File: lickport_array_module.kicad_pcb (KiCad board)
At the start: 2 copper layers, 74.9 x 80.6 mm, 105 parts, among them P1 PWR_JACK_2.1x5.5_SMD_RA, SW1 SPDT_SLIDE_500A_SM, U1 DRV103, U2 DRV103, U3 DRV103, U4 DRV103, U5 DRV103, U6 DRV103, U7 DRV103, U8 DRV103, U9 DRV103

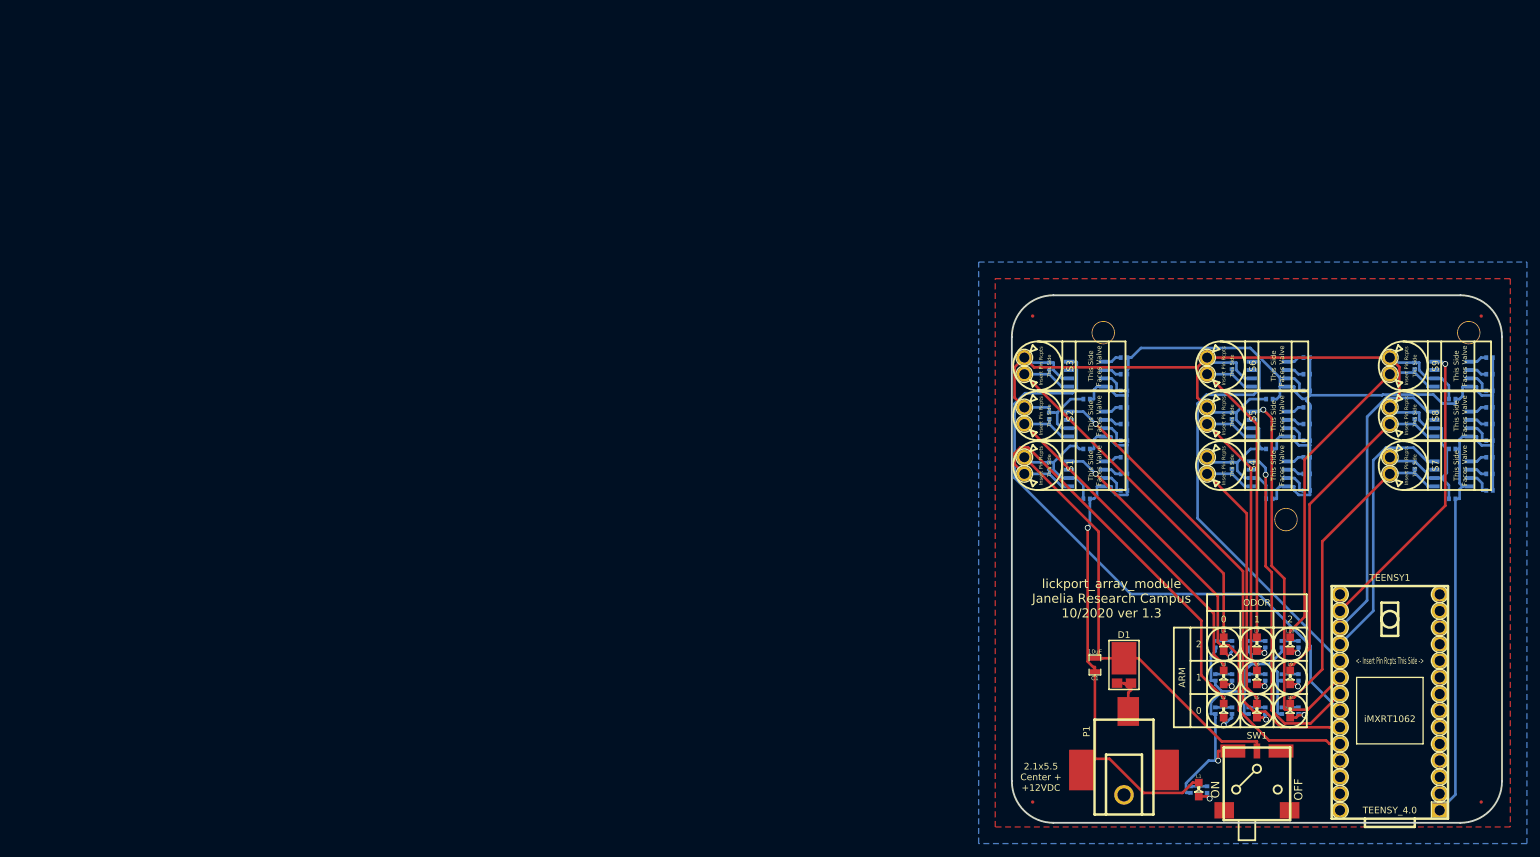
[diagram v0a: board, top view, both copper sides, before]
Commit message: Update version numbers
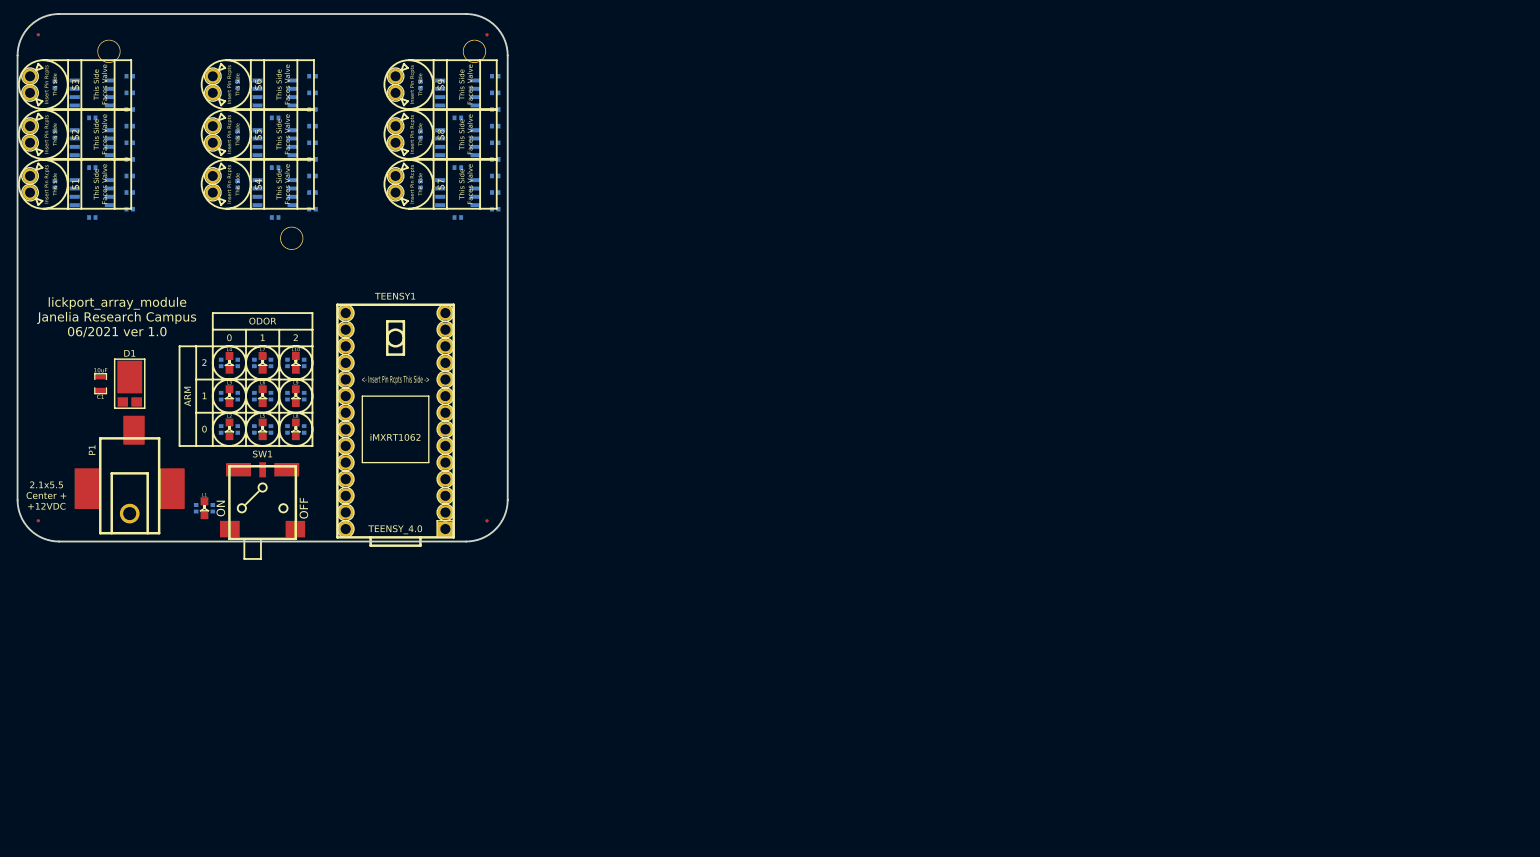
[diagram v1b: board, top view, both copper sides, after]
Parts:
- moved C1 158.0 mm to (-88.5, 64.3)
- moved C10 158.0 mm to (-61.8, 31.3)
- moved C11 158.0 mm to (-56.1, 27.5)
- moved C12 158.0 mm to (-61.8, 23.7)
- moved C13 158.0 mm to (-56.1, 19.9)
- moved C14 158.0 mm to (-33.9, 38.9)
- moved C15 158.0 mm to (-28.2, 35.1)
- moved C16 158.0 mm to (-33.9, 31.3)
- moved C17 158.0 mm to (-28.2, 27.5)
- moved C18 158.0 mm to (-33.9, 23.7)
- moved C19 158.0 mm to (-28.2, 19.9)
- moved C2 158.0 mm to (-89.8, 38.9)
- moved C3 158.0 mm to (-84.1, 35.1)
- moved C4 158.0 mm to (-89.8, 31.3)
- moved C5 158.0 mm to (-84.1, 27.5)
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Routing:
- net GND: track 300.6 -> 0.00 mm, vias 1 -> 0
- net VCC: track 286.7 -> 0.00 mm
- net /ARM_0_ODOR_2: track 94.7 -> 0.00 mm
- net /ARM_0_ODOR_1: track 73.0 -> 0.00 mm, vias 1 -> 0
- net /ARM_0_ODOR_0: track 68.3 -> 0.00 mm, vias 1 -> 0
- net /odor_0/SH: track 66.2 -> 0.00 mm
- net /ARM_1_ODOR_2: track 64.0 -> 0.00 mm
- net /Vled: track 63.4 -> 0.00 mm, vias 1 -> 0
- net /odor_2/SH: track 61.2 -> 0.00 mm
- net /ARM_1_ODOR_1: track 59.6 -> 0.00 mm, vias 1 -> 0
- net /odor_1/SH: track 58.7 -> 0.00 mm
- net /odor_8/SH: track 55.0 -> 0.00 mm
- net /ARM_1_ODOR_0: track 53.1 -> 0.00 mm, vias 1 -> 0
- net /odor_7/SH: track 52.7 -> 0.00 mm
- net /odor_5/SH: track 51.8 -> 0.00 mm
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- removed copper zone on B.Cu, net GND
- removed copper zone on F.Cu, net VCC
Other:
- board text added: "lickport_array_module Janelia Research Campus 06/2021 ver 1.0"
- board text removed: "lickport_array_module Janelia Research Campus 10/2020 ver 1.3"

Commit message: solenoid_spike_hold -> lickport_interface
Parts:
- C10, C12, C14, C16, C18, C2, C4, C6, C8, D10, D11, D12, D13, D14, D15, D16, D17, D18, D19, D20, D3, D4, D5, D6, D7, D8, D9: footprint solenoid_spike_hold:SM0402_POL -> lickport_interface:SM0402_POL
- C11, C13, C15, C17, C19, C3, C5, C7, C9, R10, R11, R12, R13, R14, R15, R16, R17, R18, R19, R2, R20, R21, R22, R23, R24, R25, R26, R27, R28, R3, R4, R5, R6, R7, R8, R9: footprint solenoid_spike_hold:SM0402 -> lickport_interface:SM0402
- L10, L2, L3, L4, L5, L6, L7, L8, L9: footprint solenoid_spike_hold:LED0805 -> lickport_interface:LED0805
- S1, S2, S3, S4, S5, S6, S7, S8, S9: footprint solenoid_spike_hold:LEECO_LHDB -> lickport_interface:LEECO_LHDB
- U1, U2, U3, U4, U5, U6, U7, U8, U9: footprint solenoid_spike_hold:SOIC_8 -> lickport_interface:SOIC_8
